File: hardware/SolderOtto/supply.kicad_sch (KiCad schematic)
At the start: 77 parts, among them J201 Conn_02x04_Counter_Clockwise, Q201 T2N7002AK, Q202 BC858B, Q203 BC847A, Q204 BC847A, U201 LM5012, U202 AP3211K, U203 AP3211K, U204 AP3211K, U205 LM27761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

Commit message: save wip
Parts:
- D206: Mouser 497-2522-1-ND -> 511-BAT54SFILM
- D207: Mouser (none) -> 511-BAT54SFILM
- JS201: Digikey 668-SMI-1027-T-5V-RCT-ND -> 668-SMI-1027-T-5V-RDKR-ND
- U206: Digikey MCP9701T-E/TTCT-ND -> MCP9701T-E/TTDKR-ND
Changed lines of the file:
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@@
 			)
 		)
-		(property "Mouser" "497-2522-1-ND"
+		(property "Mouser" "511-BAT54SFILM"
 			(at 165.354 182.118 90)
 			(effects
@@
 			)
 		)
+		(property "Mouser" "511-BAT54SFILM"
+			(at 101.6 173.99 0)
+			(effects
+				(font
+					(size 1.27 1.27)
+				)
+			)
+		)
 		(pin "3"
 		)
@@
 			)
 		)
-		(property "Digikey" "MCP9701T-E/TTCT-ND"
+		(property "Digikey" "MCP9701T-E/TTDKR-ND"
 			(at 150.368 181.102 0)
 			(effects
@@
 			)
 		)
-		(property "Datasheet" "https://www.diodes.com/assets/Datasheets/ds30849.pdf"
+		(property "Datasheet" "~"
 			(at 228.6 30.48 0)
 			(effects
@@
 			)
 		)
-		(property "Digikey" "668-SMI-1027-T-5V-RCT-ND"
+		(property "Digikey" "668-SMI-1027-T-5V-RDKR-ND"
 			(at 266.7 125.7299 0)
 			(effects

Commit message: wip
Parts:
- added BT201: Battery_Cell, Battery:BatteryHolder_LINX_BAT-HLD-012-SMT, symbol Device:Battery_Cell
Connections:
- net GND: now also BT201.2 (-)
- new net VBAT: BT201.1 (+)
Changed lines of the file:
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@@
 	(wire
 		(pts
+			(xy 57.15 31.75) (xy 57.15 27.94)
+		)
+		(stroke
+			(width 0)
+			(type default)
+		)
+	)
+	(wire
+		(pts
 			(xy 90.17 173.99) (xy 101.6 173.99)
 		)
@@
 	(wire
 		(pts
+			(xy 57.15 39.37) (xy 57.15 43.18)
+		)
+		(stroke
+			(width 0)
+			(type default)
+		)
+	)
+	(wire
+		(pts
 			(xy 36.83 41.91) (xy 36.83 45.72)
 		)
@@
 	)
 	(symbol
+		(lib_id "Device:Battery_Cell")
+		(at 57.15 36.83 0)
+		(unit 1)
+		(exclude_from_sim no)
+		(in_bom yes)
+		(on_board yes)
+		(dnp no)
+		(fields_autoplaced yes)
+		(property "Reference" "BT201"
+			(at 60.96 33.7184 0)
+			(effects
+				(font
+					(size 1.27 1.27)
+				)
+				(justify left)
+			)
+		)
+		(property "Value" "Battery_Cell"
+			(at 60.96 36.2584 0)
+			(effects
+				(font
+					(size 1.27 1.27)
+				)
+				(justify left)
+			)
+		)
+		(property "Footprint" "Battery:BatteryHolder_LINX_BAT-HLD-012-SMT"
+			(at 57.15 35.306 90)
+			(effects
+				(font
+					(size 1.27 1.27)
+				)
+				(hide yes)
+			)
+		)
+		(property "Datasheet" "~"
+			(at 57.15 35.306 90)
+			(effects
+				(font
+					(size 1.27 1.27)
+				)
+				(hide yes)
+			)
+		)
+		(property "Description" "Single-cell battery"
+			(at 57.15 36.83 0)
+			(effects
+				(font
+					(size 1.27 1.27)
+				)
+				(hide yes)
+			)
+		)
+		(property "Digikey" "BAT-HLD-012-SMT-ND"
+			(at 57.15 36.83 0)
+			(effects
+				(font
+					(size 1.27 1.27)
+				)
+				(hide yes)
+			)
+		)
+		(pin "2"
+		)
+		(pin "1"
+		)
+		(instances
+			(project "SolderOtto"
+				(path "/04e99464-bf33-4a4f-8397-d26b5ec904f3/1f74b07f-4a28-48ba-be90-ad5de8d466f3"
+					(reference "BT201")
+					(unit 1)
+				)
+			)
+		)
+	)
+	(symbol
 		(lib_id "mylib_diodes:BAT54SFILM")
 		(at 163.83 172.72 90)
@@
 	)
 	(symbol
+		(lib_id "mylib_power:VBAT")
+		(at 57.15 27.94 0)
+		(unit 1)
+		(exclude_from_sim no)
+		(in_bom yes)
+		(on_board yes)
+		(dnp no)
+		(fields_autoplaced yes)
+		(property "Reference" "#PWR0264"
+			(at 57.15 31.75 0)
+			(effects
+				(font
+					(size 1.27 1.27)
+				)
+				(hide yes)
+			)
+		)
+		(property "Value" "VBAT"
+			(at 57.15 22.86 0)
+			(effects
+				(font
+					(size 1.27 1.27)
+				)
+			)
+		)
+		(property "Footprint" ""
+			(at 57.15 27.94 0)
+			(effects
+				(font
+					(size 1.27 1.27)
+				)
+				(hide yes)
+			)
+		)
+		(property "Datasheet" ""
+			(at 57.15 27.94 0)
+			(effects
+				(font
+					(size 1.27 1.27)
+				)
+				(hide yes)
+			)
+		)
+		(property "Description" "Power symbol creates a global label with name \"VBAT\""
+			(at 57.15 27.94 0)
+			(effects
+				(font
+					(size 1.27 1.27)
+				)
+				(hide yes)
+			)
+		)
+		(pin "1"
+		)
+		(instances
+			(project "SolderOtto"
+				(path "/04e99464-bf33-4a4f-8397-d26b5ec904f3/1f74b07f-4a28-48ba-be90-ad5de8d466f3"
+					(reference "#PWR0264")
+					(unit 1)
+				)
+			)
+		)
+	)
+	(symbol
 		(lib_id "power:+3V3")
 		(at 101.6 161.29 0)
@@
 					(unit 1)
 				)
+			)
+		)
+	)
+	(symbol
+		(lib_id "power:GND")
+		(at 57.15 43.18 0)
+		(unit 1)
+		(exclude_from_sim no)
+		(in_bom yes)
+		(on_board yes)
+		(dnp no)
+		(property "Reference" "#PWR0265"
+			(at 57.15 49.53 0)
+			(effects
+				(font
+					(size 1.27 1.27)
+				)
+				(hide yes)
+			)
+		)
+		(property "Value" "GND"
+			(at 57.277 47.5742 0)
+			(effects
+				(font
+					(size 1.27 1.27)
+				)
+			)
+		)
+		(property "Footprint" ""
+			(at 57.15 43.18 0)
+			(effects
+				(font
+					(size 1.27 1.27)
+				)
+				(hide yes)
+			)
+		)
+		(property "Datasheet" ""
+			(at 57.15 43.18 0)
+			(effects
+				(font
+					(size 1.27 1.27)
+				)
+				(hide yes)
+			)
+		)
+		(property "Description" "Power symbol creates a global label with name \"GND\" , ground"
+			(at 57.15 43.18 0)
+			(effects
+				(font
+					(size 1.27 1.27)
+				)
+				(hide yes)
+			)
+		)
+		(pin "1"
+		)
+		(instances
+			(project "SolderOtto"
+				(path "/04e99464-bf33-4a4f-8397-d26b5ec904f3/1f74b07f-4a28-48ba-be90-ad5de8d466f3"
+					(reference "#PWR0265")
+					(unit 1)
+				)

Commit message: save wip
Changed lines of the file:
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@@
 	)
 	(junction
+		(at 57.15 30.48)
+		(diameter 0)
+		(color 0 0 0 0)
+	)
+	(junction
 		(at 40.64 45.72)
 		(diameter 0)
@@
 	(wire
 		(pts
+			(xy 66.04 26.67) (xy 66.04 30.48)
+		)
+		(stroke
+			(width 0)
+			(type default)
+		)
+	)
+	(wire
+		(pts
 			(xy 50.8 170.18) (xy 50.8 156.21)
 		)
@@
 	(wire
 		(pts
+			(xy 57.15 30.48) (xy 57.15 27.94)
+		)
+		(stroke
+			(width 0)
+			(type default)
+		)
+	)
+	(wire
+		(pts
 			(xy 68.58 151.13) (xy 71.12 151.13)
 		)
@@
 	(wire
 		(pts
-			(xy 57.15 31.75) (xy 57.15 27.94)
+			(xy 57.15 31.75) (xy 57.15 30.48)
 		)
 		(stroke
@@
 	(wire
 		(pts
+			(xy 66.04 30.48) (xy 57.15 30.48)
+		)
+		(stroke
+			(width 0)
+			(type default)
+		)
+	)
+	(wire
+		(pts
 			(xy 247.65 127) (xy 247.65 129.54)
 		)
@@
 					(unit 1)
 				)
+			)
+		)
+	)
+	(symbol
+		(lib_id "power:PWR_FLAG")
+		(at 66.04 26.67 0)
+		(unit 1)
+		(exclude_from_sim no)
+		(in_bom yes)
+		(on_board yes)
+		(dnp no)
+		(property "Reference" "#FLG0210"
+			(at 66.04 24.765 0)
+			(effects
+				(font
+					(size 1.27 1.27)
+				)
+				(hide yes)
+			)
+		)
+		(property "Value" "PWR_FLAG"
+			(at 66.04 22.352 0)
+			(effects
+				(font
+					(size 1.27 1.27)
+				)
+			)
+		)
+		(property "Footprint" ""
+			(at 66.04 26.67 0)
+			(effects
+				(font
+					(size 1.27 1.27)
+				)
+				(hide yes)
+			)
+		)
+		(property "Datasheet" "~"
+			(at 66.04 26.67 0)
+			(effects
+				(font
+					(size 1.27 1.27)
+				)
+				(hide yes)
+			)
+		)
+		(property "Description" "Special symbol for telling ERC where power comes from"
+			(at 66.04 26.67 0)
+			(effects
+				(font
+					(size 1.27 1.27)
+				)
+				(hide yes)
+			)
+		)
+		(pin "1"
+		)
+		(instances
+			(project "SolderOtto"
+				(path "/04e99464-bf33-4a4f-8397-d26b5ec904f3/1f74b07f-4a28-48ba-be90-ad5de8d466f3"
+					(reference "#FLG0210")
+					(unit 1)
+				)

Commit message: fix electrical findings
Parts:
- added TP208: ZCD, TestPoint:TestPoint_Keystone_5015_Micro-Minature, symbol Connector:TestPoint
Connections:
- net GND: now also TP208.1
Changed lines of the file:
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@@
 	)
 	(junction
+		(at 19.05 45.72)
+		(diameter 0)
+		(color 0 0 0 0)
+	)
+	(junction
 		(at 223.52 71.12)
 		(diameter 0)
@@
 	(wire
 		(pts
+			(xy 19.05 44.45) (xy 19.05 45.72)
+		)
+		(stroke
+			(width 0)
+			(type default)
+		)
+	)
+	(wire
+		(pts
 			(xy 40.64 130.81) (xy 40.64 133.35)
 		)
@@
 	(wire
 		(pts
-			(xy 166.37 35.56) (xy 166.37 38.1)
-		)
-		(stroke
-			(width 0)
-			(type default)
-		)
-	)
-	(wire
-		(pts
 			(xy 170.18 124.46) (xy 170.18 125.73)
 		)
@@
 	(wire
 		(pts
-			(xy 19.05 44.45) (xy 19.05 45.72)
+			(xy 101.6 173.99) (xy 110.49 173.99)
 		)
 		(stroke
@@
 	(wire
 		(pts
-			(xy 101.6 173.99) (xy 110.49 173.99)
+			(xy 166.37 35.56) (xy 166.37 38.1)
 		)
 		(stroke
@@
 	)
 	(symbol
+		(lib_id "Connector:TestPoint")
+		(at 19.05 45.72 180)
+		(unit 1)
+		(exclude_from_sim no)
+		(in_bom yes)
+		(on_board yes)
+		(dnp no)
+		(property "Reference" "TP208"
+			(at 22.098 51.308 0)
+			(effects
+				(font
+					(size 1.27 1.27)
+				)
+				(justify left)
+			)
+		)
+		(property "Value" "ZCD"
+			(at 16.51 47.7521 0)
+			(effects
+				(font
+					(size 1.27 1.27)
+				)
+				(justify left)
+				(hide yes)
+			)
+		)
+		(property "Footprint" "TestPoint:TestPoint_Keystone_5015_Micro-Minature"
+			(at 13.97 45.72 0)
+			(effects
+				(font
+					(size 1.27 1.27)
+				)
+				(hide yes)
+			)
+		)
+		(property "Datasheet" "~"
+			(at 13.97 45.72 0)
+			(effects
+				(font
+					(size 1.27 1.27)
+				)
+				(hide yes)
+			)
+		)
+		(property "Description" "test point"
+			(at 19.05 45.72 0)
+			(effects
+				(font
+					(size 1.27 1.27)
+				)
+				(hide yes)
+			)
+		)
+		(property "Digikey" "36-5015CT-ND"
+			(at 19.05 45.72 0)
+			(effects
+				(font
+					(size 1.27 1.27)
+				)
+				(hide yes)
+			)
+		)
+		(pin "1"
+		)
+		(instances
+			(project "SolderOtto"
+				(path "/04e99464-bf33-4a4f-8397-d26b5ec904f3/1f74b07f-4a28-48ba-be90-ad5de8d466f3"
+					(reference "TP208")
+					(unit 1)
+				)
+			)
+		)
+	)
+	(symbol
 		(lib_id "power:GND")
 		(at 223.52 91.44 0)
@@
 	)
 	(symbol
-		(lib_id "power:PWR_FLAG")
-		(at 19.05 44.45 0)
-		(unit 1)
-		(exclude_from_sim no)
-		(in_bom yes)
-		(on_board yes)
-		(dnp no)
-		(property "Reference" "#FLG0205"
-			(at 19.05 42.545 0)
-			(effects
-				(font
-					(size 1.27 1.27)
-				)
-				(hide yes)
-			)
-		)
-		(property "Value" "PWR_FLAG"
-			(at 19.05 39.37 0)
-			(effects
-				(font
-					(size 1.27 1.27)
-				)
-			)
-		)
-		(property "Footprint" ""
-			(at 19.05 44.45 0)
-			(effects
-				(font
-					(size 1.27 1.27)
-				)
-				(hide yes)
-			)
-		)
-		(property "Datasheet" "~"
-			(at 19.05 44.45 0)
-			(effects
-				(font
-					(size 1.27 1.27)
-				)
-				(hide yes)
-			)
-		)
-		(property "Description" "Special symbol for telling ERC where power comes from"
-			(at 19.05 44.45 0)
-			(effects
-				(font
-					(size 1.27 1.27)
-				)
-				(hide yes)
-			)
-		)
-		(pin "1"
-		)
-		(instances
-			(project "SolderOtto"
-				(path "/04e99464-bf33-4a4f-8397-d26b5ec904f3/1f74b07f-4a28-48ba-be90-ad5de8d466f3"
-					(reference "#FLG0205")
-					(unit 1)
-				)
-			)
-		)
-	)
-	(symbol
 		(lib_id "Device:R")
 		(at 243.84 25.4 270)
@@
 					(unit 1)
 				)
+			)
+		)
+	)
+	(symbol
+		(lib_id "power:PWR_FLAG")
+		(at 19.05 44.45 0)
+		(unit 1)
+		(exclude_from_sim no)
+		(in_bom yes)
+		(on_board yes)
+		(dnp no)
+		(property "Reference" "#FLG0205"
+			(at 19.05 42.545 0)
+			(effects
+				(font
+					(size 1.27 1.27)
+				)
+				(hide yes)
+			)
+		)
+		(property "Value" "PWR_FLAG"
+			(at 19.05 40.132 0)
+			(effects
+				(font
+					(size 1.27 1.27)
+				)
+			)
+		)
+		(property "Footprint" ""
+			(at 19.05 44.45 0)
+			(effects
+				(font
+					(size 1.27 1.27)
+				)
+				(hide yes)
+			)
+		)
+		(property "Datasheet" "~"
+			(at 19.05 44.45 0)
+			(effects
+				(font
+					(size 1.27 1.27)
+				)
+				(hide yes)
+			)
+		)
+		(property "Description" "Special symbol for telling ERC where power comes from"
+			(at 19.05 44.45 0)
+			(effects
+				(font
+					(size 1.27 1.27)
+				)
+				(hide yes)
+			)
+		)
+		(pin "1"
+		)
+		(instances
+			(project "SolderOtto"
+				(path "/04e99464-bf33-4a4f-8397-d26b5ec904f3/1f74b07f-4a28-48ba-be90-ad5de8d466f3"
+					(reference "#FLG0205")
+					(unit 1)
+				)

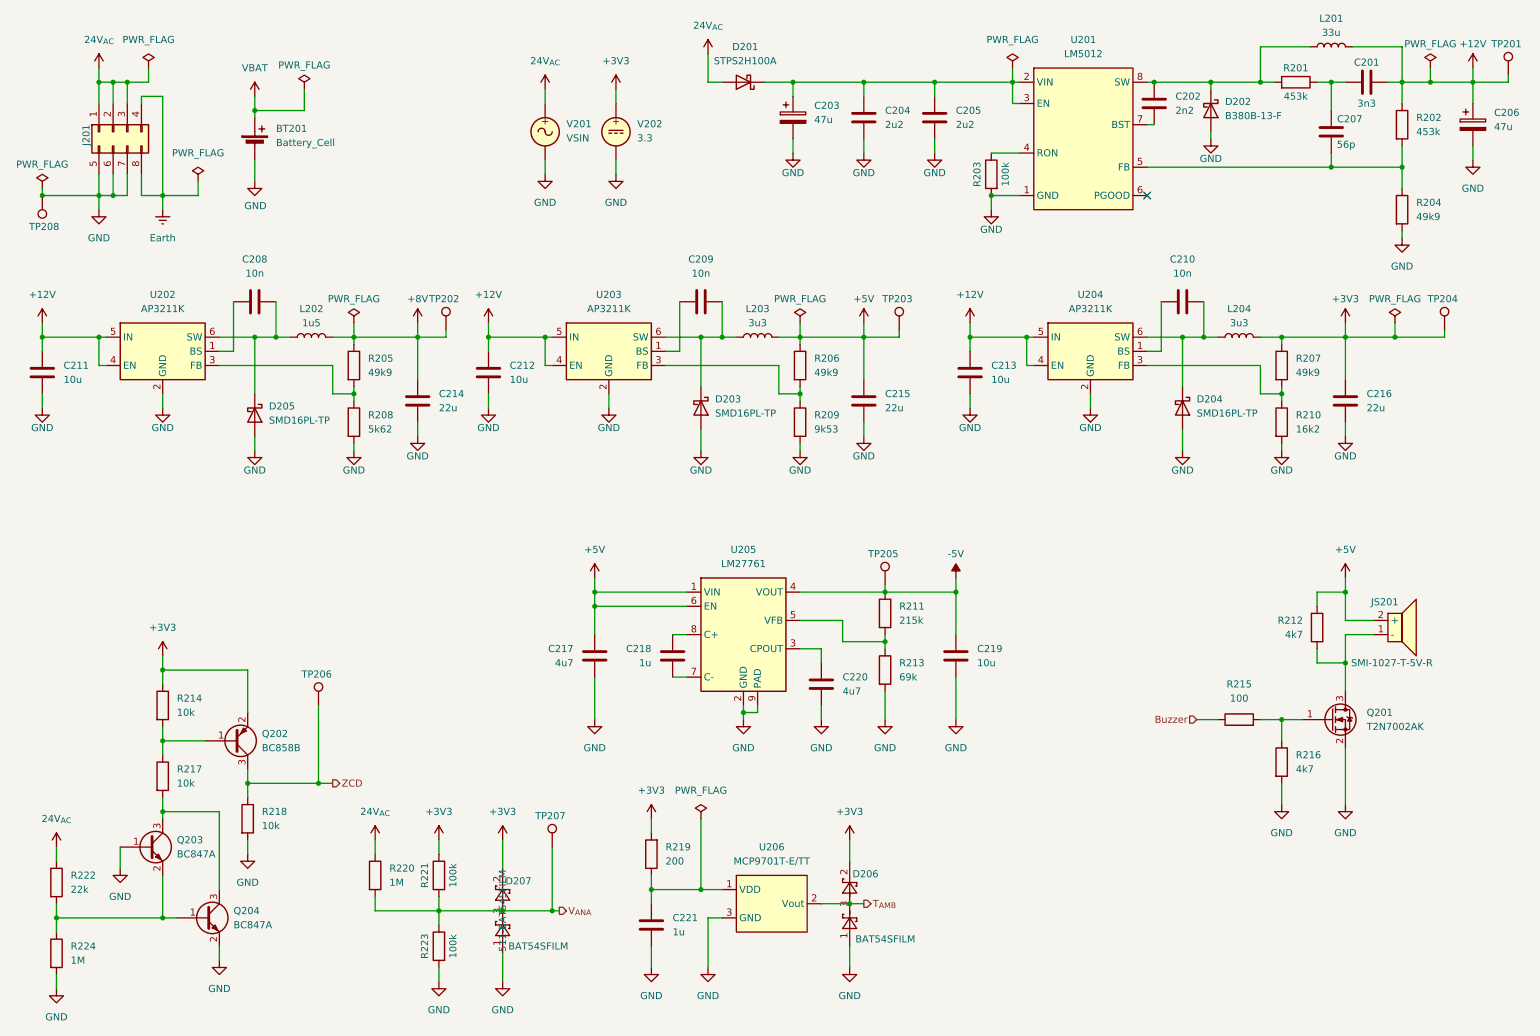
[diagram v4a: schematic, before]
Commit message: create adapter to enclosure for display
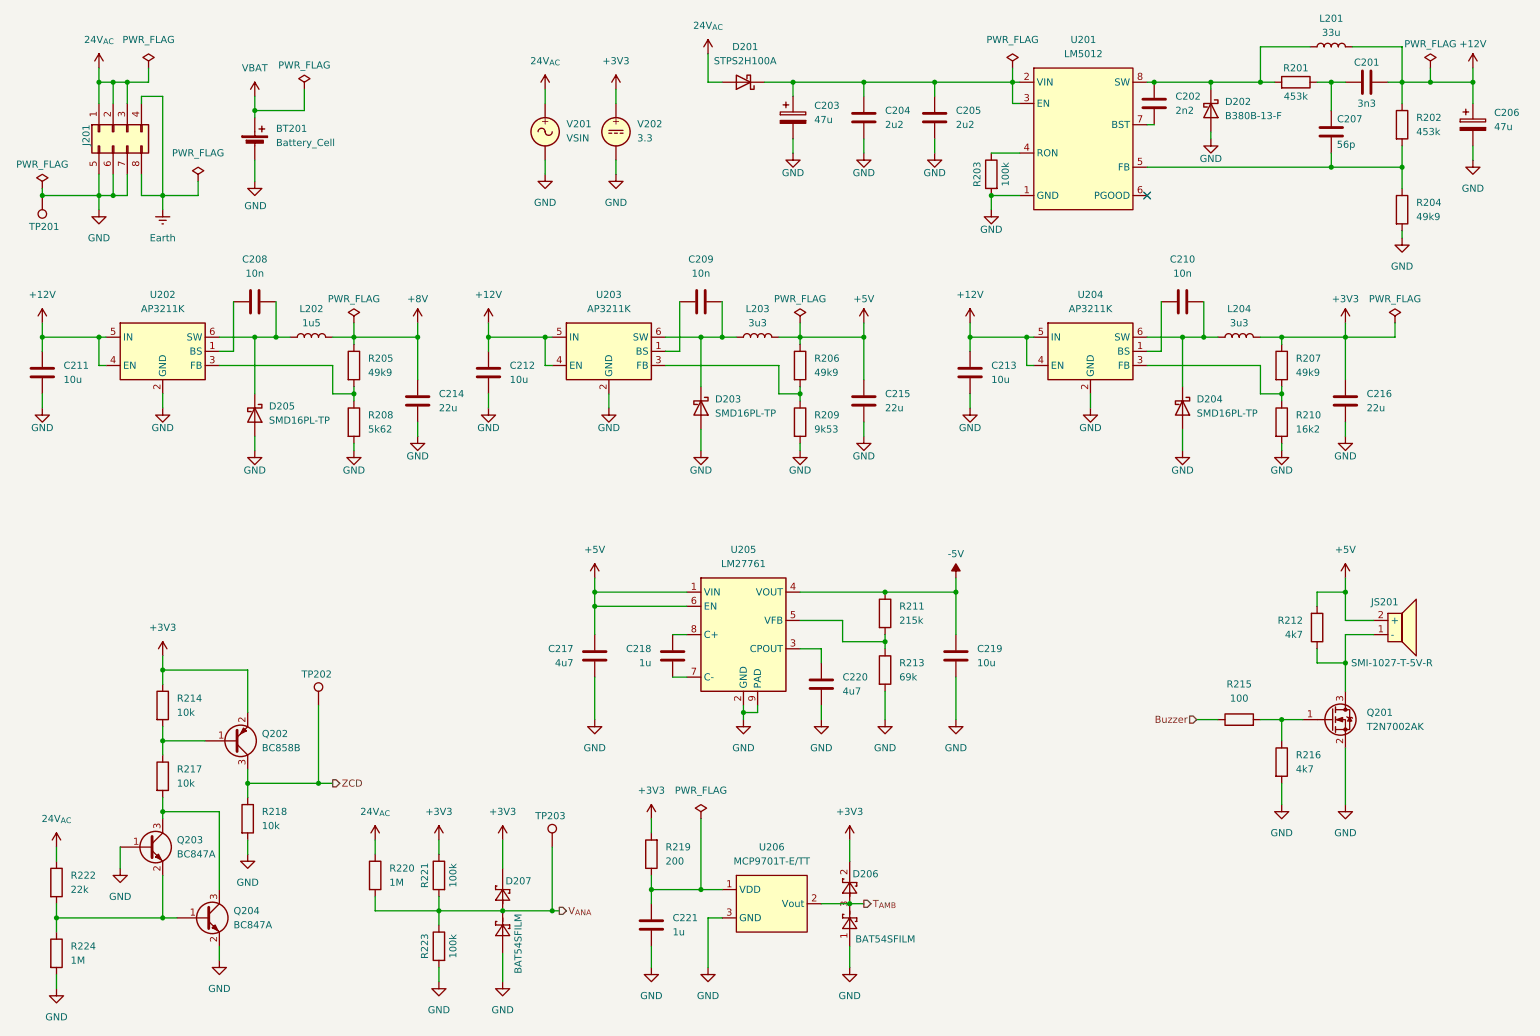
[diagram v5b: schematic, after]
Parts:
- removed TP201, TP202, TP203, TP204, TP205: ZCD, TestPoint:TestPoint_Keystone_5015_Micro-Minature, symbol Connector:TestPoint
- TP201: renamed from TP208; footprint TestPoint:TestPoint_Keystone_5015_Micro-Minature -> TestPoint:TestPoint_Keystone_5019_Minature; Digikey 36-5015CT-ND -> 36-5019CT-ND
- renumbered TP206 to TP202, TP207 to TP203
